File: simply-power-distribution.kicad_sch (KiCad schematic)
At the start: 0 parts

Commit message: done schematic
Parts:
- added H1, H2: M2.5, MountingHole:MountingHole_2.7mm_M2.5, symbol Mechanical:MountingHole
- added J1: 55-21 Barrel Jack, Connector_BarrelJack:BarrelJack_Horizontal, symbol Connector:Barrel_Jack_MountingPin
- added J2: Power distribution, Connector_PinSocket_2.54mm:PinSocket_2x09_P2.54mm_Vertical, symbol Connector_Generic:Conn_02x09_Counter_Clockwise
- added SW1: Power Switch, commons-interconnect_THT:g-switch_22f12-gxxx, symbol Switch:SW_Push_DPDT
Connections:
- new net: J1.1, SW1.2 (B)
- new net: J1.2, SW1.5 (B)
- new net: J2.1 (Pin_1), J2.2 (Pin_2), J2.3 (Pin_3), J2.4 (Pin_4), J2.5 (Pin_5), J2.6 (Pin_6), J2.7 (Pin_7), J2.8 (Pin_8), J2.9 (Pin_9), SW1.3 (C)
- new net: J2.10 (Pin_10), J2.11 (Pin_11), J2.12 (Pin_12), J2.13 (Pin_13), J2.14 (Pin_14), J2.15 (Pin_15), J2.16 (Pin_16), J2.17 (Pin_17), J2.18 (Pin_18), SW1.6 (C)
- no-connect marks 0 -> 3
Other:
- note added: "From battery holder, power adapter, etc..."
- note added: "Mounting holes"

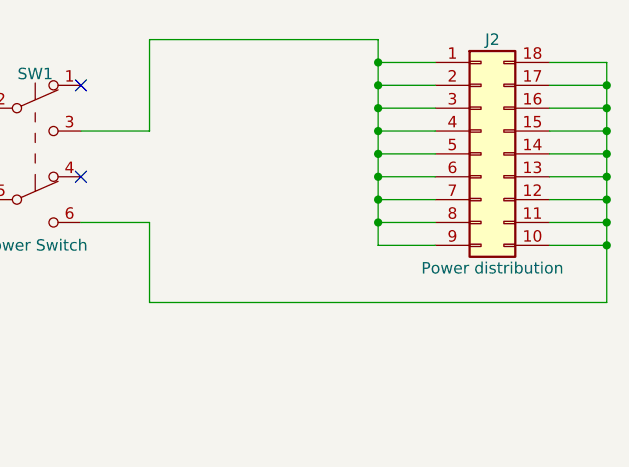
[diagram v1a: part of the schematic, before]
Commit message: pcb -- traces and markings
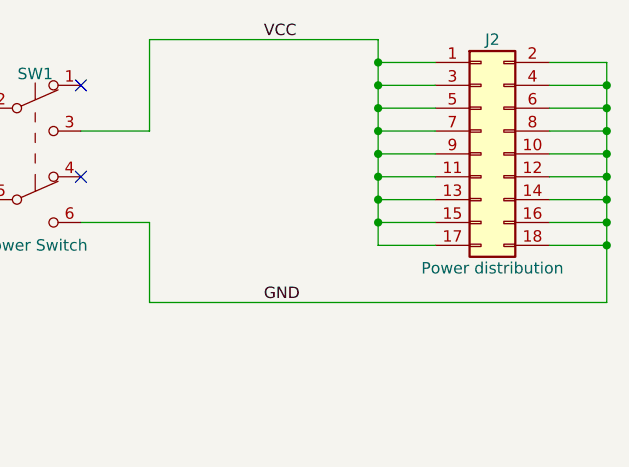
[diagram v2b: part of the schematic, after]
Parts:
- J2: symbol Connector_Generic:Conn_02x09_Counter_Clockwise -> Connector_Generic:Conn_02x09_Odd_Even
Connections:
- net VCC: now reaches J2.1 (Pin_1), J2.3 (Pin_3), J2.5 (Pin_5), J2.7 (Pin_7), J2.9 (Pin_9), SW1.3 (C)
- net VCC: now also J2.11 (Pin_11), J2.13 (Pin_13), J2.15 (Pin_15), J2.17 (Pin_17); no longer J2.2 (Pin_2), J2.4 (Pin_4), J2.6 (Pin_6), J2.8 (Pin_8)
- net GND: now reaches J2.10 (Pin_10), J2.12 (Pin_12), J2.14 (Pin_14), J2.16 (Pin_16), J2.18 (Pin_18), SW1.6 (C)
- net GND: now also J2.2 (Pin_2), J2.4 (Pin_4), J2.6 (Pin_6), J2.8 (Pin_8); no longer J2.11 (Pin_11), J2.13 (Pin_13), J2.15 (Pin_15), J2.17 (Pin_17)
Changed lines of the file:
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@@
+    (effects (font (size 1.27 1.27)) (justify left bottom))
+  )
+  (label "VCC" (at 127 38.1 0) (fields_autoplaced)
+    (effects (font (size 1.27 1.27)) (justify left bottom))
+  )
+  (label "GND" (at 127 67.31 0) (fields_autoplaced)
     (effects (font (size 1.27 1.27)) (justify left bottom))
   )
@@
     )
   )
-  (symbol (lib_id "Connector_Generic:Conn_02x09_Counter_Clockwise") (at 151.13 50.8 0) (unit 1)
+  (symbol (lib_id "Connector_Generic:Conn_02x09_Odd_Even") (at 151.13 50.8 0) (unit 1)
     (in_bom yes) (on_board yes) (dnp no)
     (property "Reference" "J2" (at 152.4 38.1 0)
